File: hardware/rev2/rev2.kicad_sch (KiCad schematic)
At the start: 30 parts, among them J1 SMA, J2 SMA, J3 SMA, J4 Antenna RF and GNSS Data, J5 Antenna GND, J7 USB_C_Receptacle_USB2.0_16P

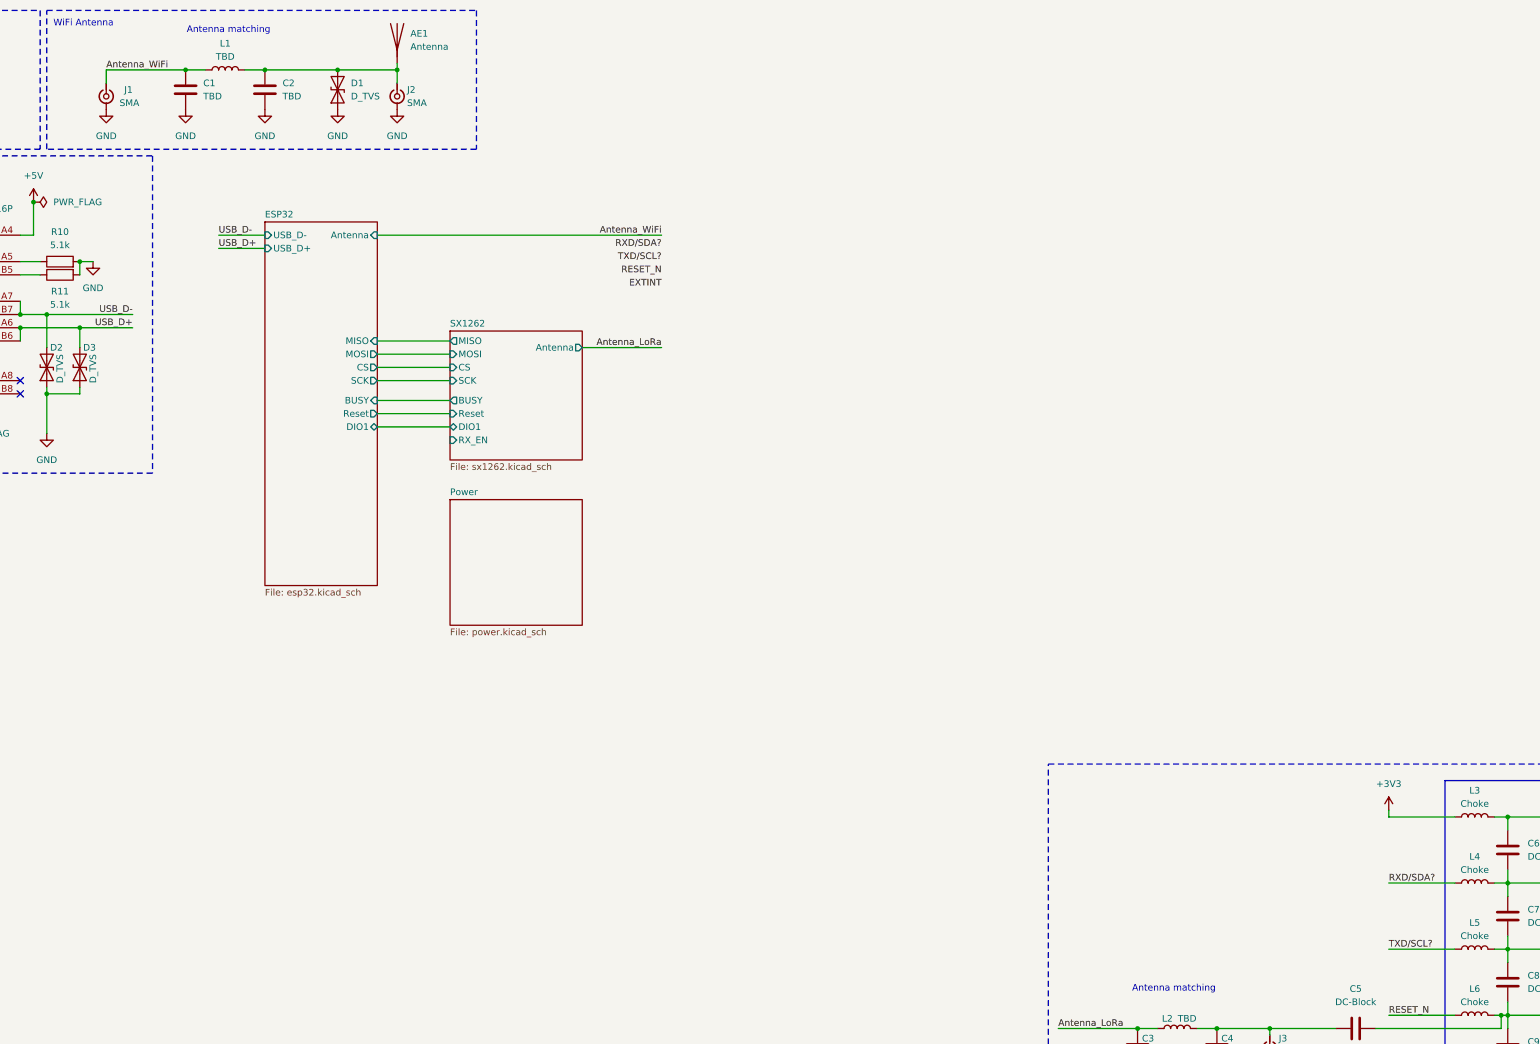
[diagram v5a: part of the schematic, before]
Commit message: ESP32 approaching final schematic. tidied up a lot and changed GPIO pins.
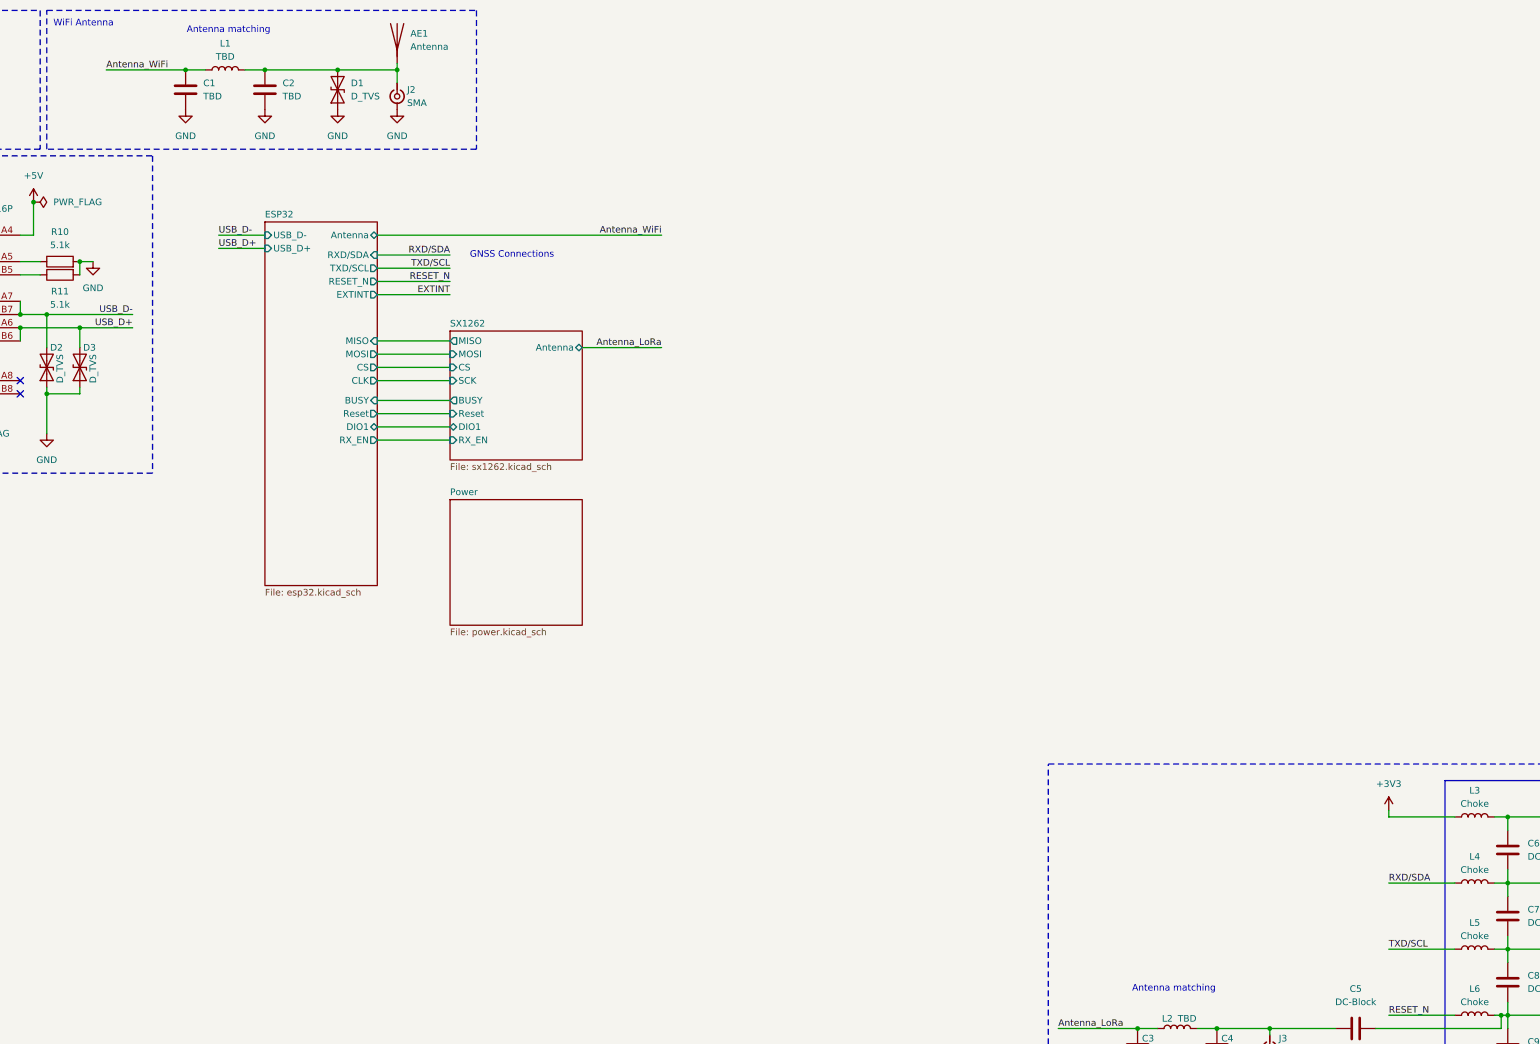
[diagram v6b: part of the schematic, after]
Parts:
- removed J1: SMA, symbol Connector:Conn_Coaxial_Small
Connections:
- net RXD/SDA? renamed RXD/SDA
- net TXD/SCL? renamed TXD/SCL
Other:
- sheet ESP32 ports: added CLK, EXTINT, RESET_N, RXD/SDA, RX_EN, TXD/SCL; removed SCK
- note added: "GNSS Connections"
- company: (none) -> MMCX11
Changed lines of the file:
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@@
 	(generator_version "10.0")
 	(paper "A3")
+	(title_block
+		(company "MMCX11")
+	)
 	(rectangle
 		(start 13.97 41.91)
@@
 		)
 	)
+	(text "GNSS Connections"
+		(exclude_from_sim no)
+		(at 133.35 60.96 0)
+		(effects
+			(font
+				(size 1.27 1.27)
+			)
+			(justify left)
+		)
+	)
 	(junction
 		(at 332.74 168.91)
@@
 	(wire
 		(pts
+			(xy 115.57 96.52) (xy 129.54 96.52)
+		)
+		(stroke
+			(width 0)
+			(type default)
+		)
+	)
+	(wire
+		(pts
 			(xy 50.8 62.23) (xy 46.99 62.23)
 		)
@@
 	(wire
 		(pts
+			(xy 115.57 66.04) (xy 129.54 66.04)
+		)
+		(stroke
+			(width 0)
+			(type default)
+		)
+	)
+	(wire
+		(pts
 			(xy 52.07 87.63) (xy 58.42 87.63)
 		)
@@
 	(wire
 		(pts
+			(xy 115.57 68.58) (xy 129.54 68.58)
+		)
+		(stroke
+			(width 0)
+			(type default)
+		)
+	)
+	(wire
+		(pts
 			(xy 287.02 209.55) (xy 299.72 209.55)
 		)
@@
 	(wire
 		(pts
-			(xy 63.5 25.4) (xy 63.5 27.94)
-		)
-		(stroke
-			(width 0)
-			(type default)
-		)
-	)
-	(wire
-		(pts
 			(xy 85.09 59.69) (xy 93.98 59.69)
 		)
@@
 	(wire
 		(pts
+			(xy 115.57 63.5) (xy 129.54 63.5)
+		)
+		(stroke
+			(width 0)
+			(type default)
+		)
+	)
+	(wire
+		(pts
 			(xy 332.74 229.87) (xy 332.74 232.41)
 		)
@@
 	(wire
 		(pts
+			(xy 115.57 60.96) (xy 129.54 60.96)
+		)
+		(stroke
+			(width 0)
+			(type default)
+		)
+	)
+	(wire
+		(pts
 			(xy 52.07 86.36) (xy 52.07 87.63)
 		)
@@
 	)
 	(label "EXTINT"
-		(at 170.18 67.31 180)
+		(at 129.54 68.58 180)
 		(effects
 			(font
@@
 		)
 	)
-	(label "RXD{slash}SDA?"
-		(at 170.18 59.69 180)
+	(label "RXD{slash}SDA"
+		(at 129.54 60.96 180)
 		(effects
 			(font
@@
 	)
 	(label "RESET_N"
-		(at 170.18 64.77 180)
+		(at 129.54 66.04 180)
 		(effects
 			(font
@@
 		)
 	)
-	(label "RXD{slash}SDA?"
+	(label "RXD{slash}SDA"
 		(at 309.88 181.61 0)
 		(effects
@@
 		)
 	)
-	(label "TXD{slash}SCL?"
+	(label "TXD{slash}SCL"
 		(at 309.88 194.31 0)
 		(effects
@@
 		)
 	)
-	(label "TXD{slash}SCL?"
-		(at 170.18 62.23 180)
+	(label "TXD{slash}SCL"
+		(at 129.54 63.5 180)
 		(effects
 			(font
@@
 	)
 	(symbol
-		(lib_id "power:GND")
-		(at 63.5 33.02 0)
-		(mirror y)
-		(unit 1)
-		(body_style 1)
-		(exclude_from_sim no)
-		(in_bom yes)
-		(on_board yes)
-		(in_pos_files yes)
-		(dnp no)
-		(fields_autoplaced yes)
-		(property "Reference" "#PWR01"
-			(at 63.5 39.37 0)
-			(hide yes)
-			(show_name no)
-			(do_not_autoplace no)
-			(effects
-				(font
-					(size 1.27 1.27)
-				)
-			)
-		)
-		(property "Value" "GND"
-			(at 63.5 38.1 0)
-			(show_name no)
-			(do_not_autoplace no)
-			(effects
-				(font
-					(size 1.27 1.27)
-				)
-			)
-		)
-		(property "Footprint" ""
-			(at 63.5 33.02 0)
-			(hide yes)
-			(show_name no)
-			(do_not_autoplace no)
-			(effects
-				(font
-					(size 1.27 1.27)
-				)
-			)
-		)
-		(property "Datasheet" ""
-			(at 63.5 33.02 0)
-			(hide yes)
-			(show_name no)
-			(do_not_autoplace no)
-			(effects
-				(font
-					(size 1.27 1.27)
-				)
-			)
-		)
-		(property "Description" "Power symbol creates a global label with name \"GND\" , ground"
-			(at 63.5 33.02 0)
-			(hide yes)
-			(show_name no)
-			(do_not_autoplace no)
-			(effects
-				(font
-					(size 1.27 1.27)
-				)
-			)
-		)
-		(pin "1"
-		)
-		(instances
-			(project "rev2"
-				(path "/9067f306-e23c-4d77-8182-4fa2c4b88902"
-					(reference "#PWR01")
-					(unit 1)
-				)
-			)
-		)
-	)
-	(symbol
 		(lib_id "Device:C")
 		(at 93.98 29.21 0)
@@
 	)
 	(symbol
-		(lib_id "Connector:Conn_Coaxial_Small")
-		(at 63.5 30.48 90)
-		(mirror x)
-		(unit 1)
-		(body_style 1)
-		(exclude_from_sim no)
-		(in_bom yes)
-		(on_board yes)
-		(in_pos_files yes)
-		(dnp no)
-		(property "Reference" "J1"
-			(at 68.58 29.21 90)
-			(show_name no)
-			(do_not_autoplace no)
-			(effects
-				(font
-					(size 1.27 1.27)
-				)
-				(justify left)
-			)
-		)
-		(property "Value" "SMA"
-			(at 69.85 31.75 90)
-			(show_name no)
-			(do_not_autoplace no)
-			(effects
-				(font
-					(size 1.27 1.27)
-				)
-				(justify left)
-			)
-		)
-		(property "Footprint" ""
-			(at 63.5 30.48 0)
-			(hide yes)
-			(show_name no)
-			(do_not_autoplace no)
-			(effects
-				(font
-					(size 1.27 1.27)
-				)
-			)
-		)
-		(property "Datasheet" ""
-			(at 63.5 30.48 0)
-			(hide yes)
-			(show_name no)
-			(do_not_autoplace no)
-			(effects
-				(font
-					(size 1.27 1.27)
-				)
-			)
-		)
-		(property "Description" "small coaxial connector (BNC, SMA, SMB, SMC, Cinch/RCA, LEMO, ...)"
-			(at 63.5 30.48 0)
-			(hide yes)
-			(show_name no)
-			(do_not_autoplace no)
-			(effects
-				(font
-					(size 1.27 1.27)
-				)
-			)
-		)
-		(pin "1"
-		)
-		(pin "2"
-		)
-		(instances
-			(project "rev2"
-				(path "/9067f306-e23c-4d77-8182-4fa2c4b88902"
-					(reference "J1")
-					(unit 1)
-				)
-			)
-		)
-	)
-	(symbol
 		(lib_id "power:+5V")
 		(at 49.53 50.8 0)
@@
 			)
 		)
-		(pin "Antenna" input
+		(pin "Antenna" bidirectional
 			(at 115.57 57.15 0)
 			(effects
@@
 			)
 		)
-		(pin "SCK" output
+		(pin "USB_D-" input
+			(at 93.98 57.15 180)
+			(effects
+				(font
+					(size 1.27 1.27)
+				)
+				(justify left)
+			)
+		)
+		(pin "USB_D+" input
+			(at 93.98 59.69 180)
+			(effects
+				(font
+					(size 1.27 1.27)
+				)
+				(justify left)
+			)
+		)
+		(pin "CLK" output
 			(at 115.57 85.09 0)
 			(effects
@@
 			)
 		)
-		(pin "USB_D-" input
-			(at 93.98 57.15 180)
+		(pin "RX_EN" output
+			(at 115.57 96.52 0)
 			(effects
 				(font
 					(size 1.27 1.27)
 				)
-				(justify left)
+				(justify right)
 			)
 		)
-		(pin "USB_D+" input
-			(at 93.98 59.69 180)
+		(pin "EXTINT" output
+			(at 115.57 68.58 0)
 			(effects
 				(font
 					(size 1.27 1.27)
 				)
-				(justify left)
+				(justify right)
+			)
+		)
+		(pin "RESET_N" output
+			(at 115.57 66.04 0)
+			(effects
+				(font
+					(size 1.27 1.27)
+				)
+				(justify right)
+			)
+		)
+		(pin "RXD{slash}SDA" input
+			(at 115.57 60.96 0)
+			(effects
+				(font
+					(size 1.27 1.27)
+				)
+				(justify right)
+			)
+		)
+		(pin "TXD{slash}SCL" output
+			(at 115.57 63.5 0)
+			(effects
+				(font
+					(size 1.27 1.27)
+				)
+				(justify right)
 			)
 		)
@@
 			)
 		)
-		(pin "Antenna" output
+		(pin "Antenna" bidirectional
 			(at 154.94 78.74 0)
 			(effects

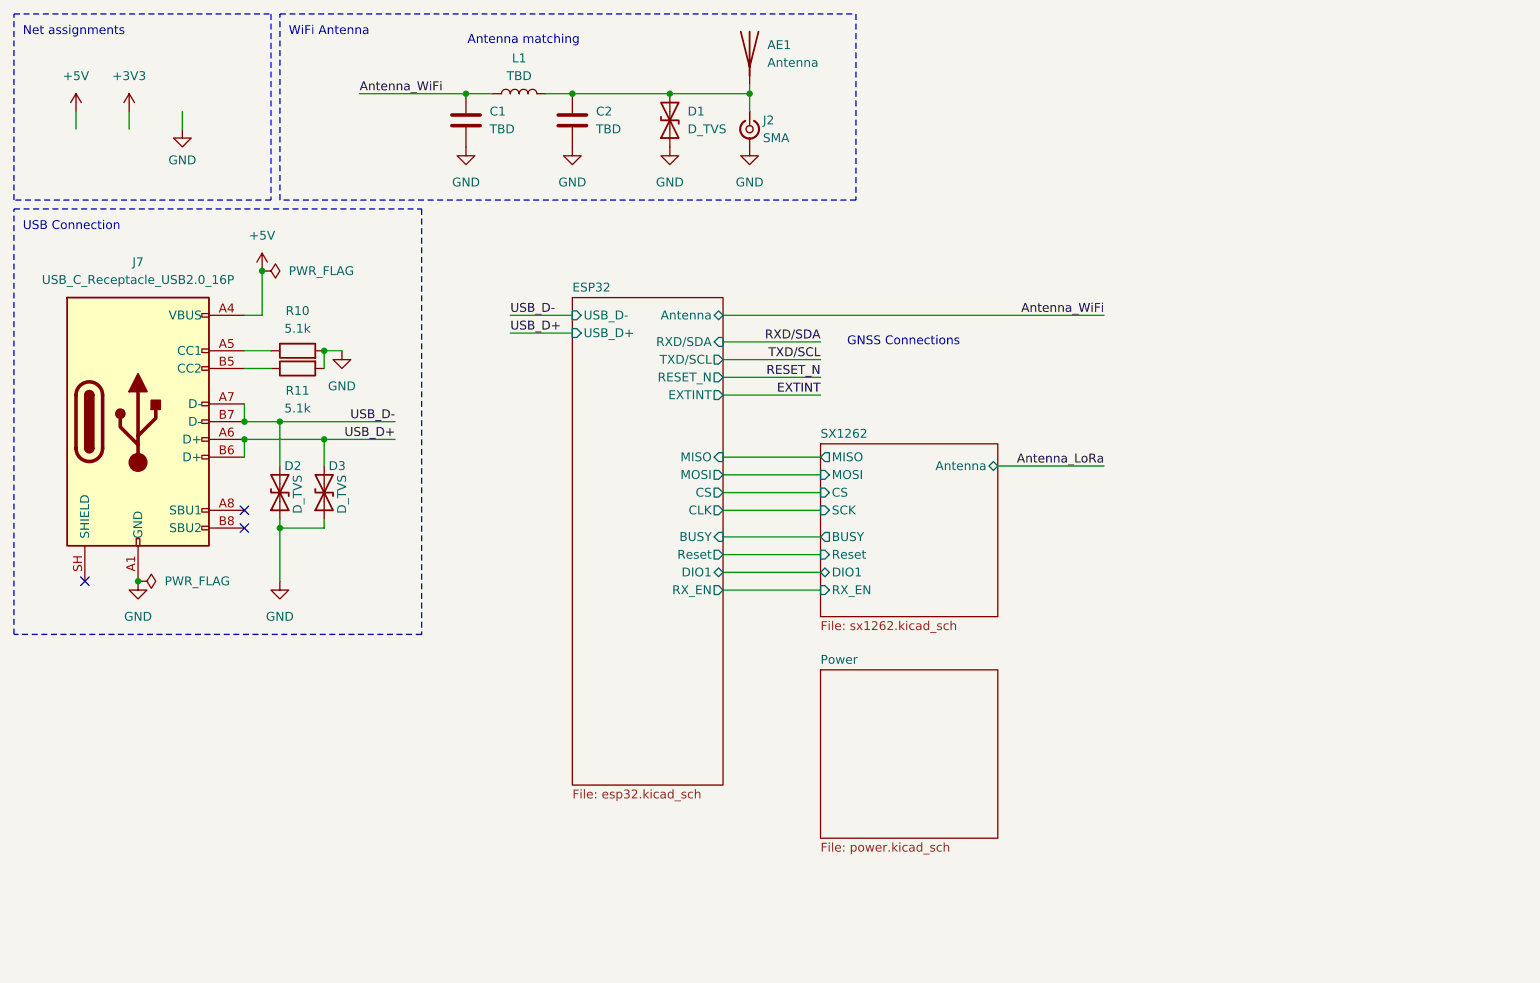
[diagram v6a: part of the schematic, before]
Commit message: redid usb termination and begun adding components from mouser
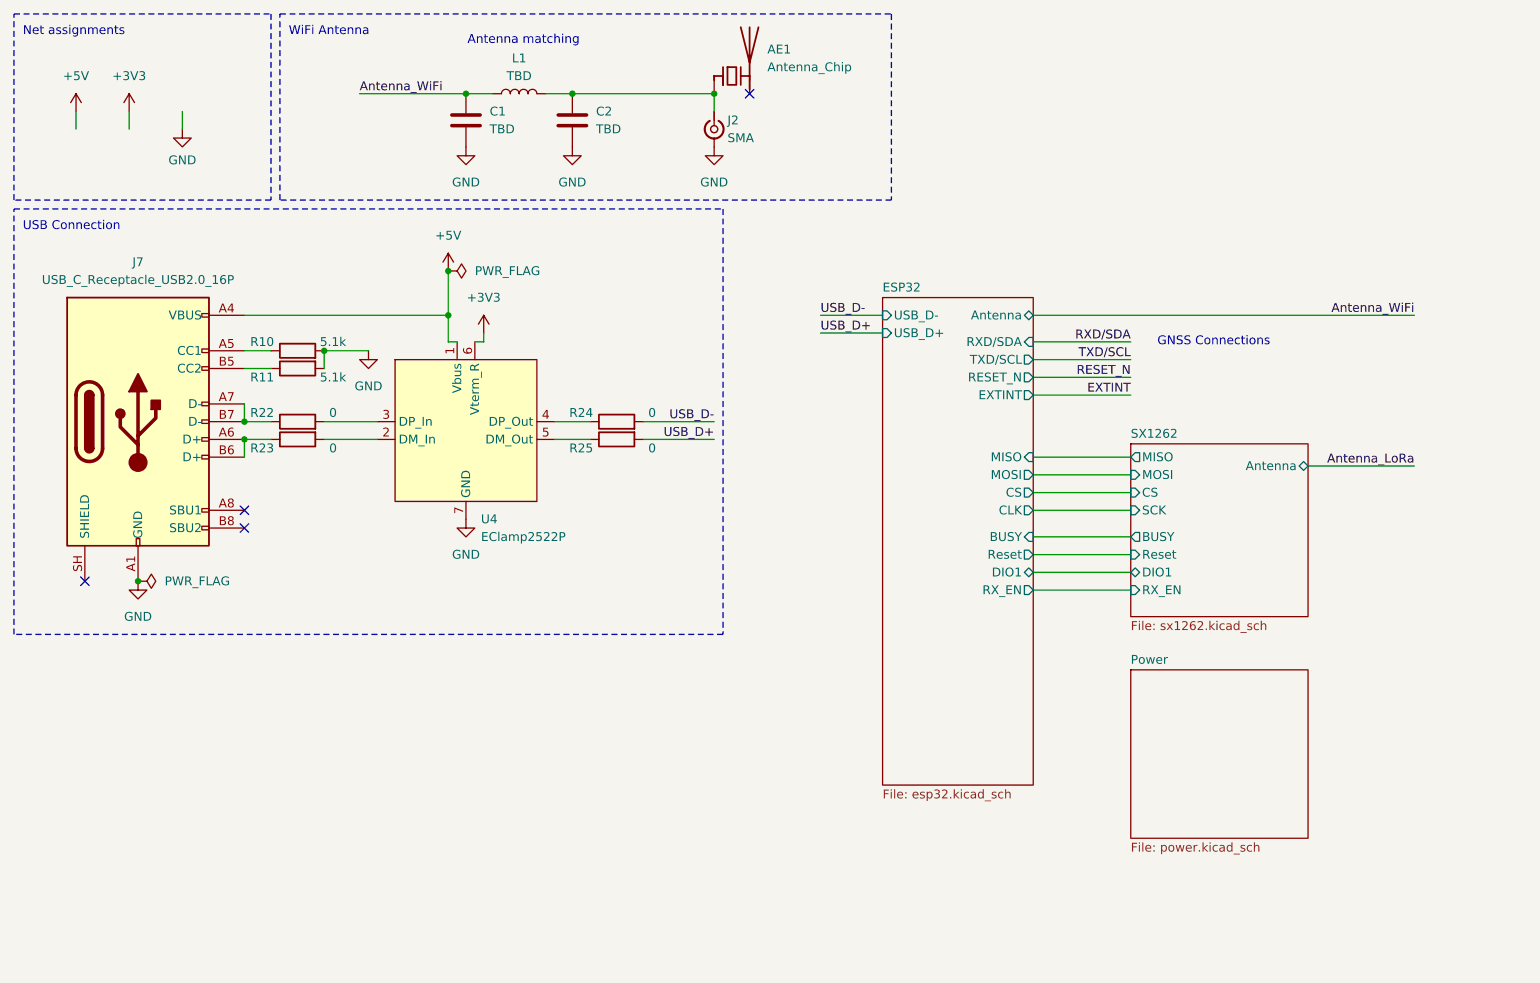
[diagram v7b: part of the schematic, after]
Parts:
- removed AE1: Antenna, symbol Device:Antenna
- removed D1, D2, D3: D_TVS, symbol Device:D_TVS
- added AE1: Antenna_Chip, _footprints:ACAG0301-2450-T, symbol Device:Antenna_Chip
- added R22, R23, R24, R25: 0, Inductor_SMD:L_0603_1608Metric_Pad1.05x0.95mm_HandSolder, symbol Device:R
- added U4: EClamp2522P, _footprints:SLP1616P6, symbol _symbols:EClamp2522P
- J2, J3: footprint (none) -> Connector_Coaxial:SMA_Amphenol_132134-16_Vertical; Mouser Part Number (none) -> 640-RFPCSMA28F
- J7: Mouser Part Number (none) -> 179-UJ20CHGSMT5P16TR
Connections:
- net +3V3: now also U4.6 (Vterm_R)
- net +5V: now also U4.1 (Vbus)
- net GND: now also U4.7 (GND)
- net USB_D+: now also R25.2; no longer J7.A6 (D+), J7.B6 (D+)
- net USB_D-: now also R24.2; no longer J7.A7 (D-), J7.B7 (D-)
- net at C2.1, J2.1 (In), L1.1: now also AE1.1 (FEED)
- new net: J7.A7 (D-), J7.B7 (D-), R22.1
- new net: R22.2, U4.3 (DP_In)
- new net: R23.2, U4.2 (DM_In)
- new net: R24.1, U4.4 (DP_Out)
- new net: R25.1, U4.5 (DM_Out)
- new net: J7.A6 (D+), J7.B6 (D+), R23.1
- no-connect marks 3 -> 4
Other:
- moved on the sheet: J2
